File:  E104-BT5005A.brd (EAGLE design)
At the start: 15.5 x 15.5 mm, 5 parts

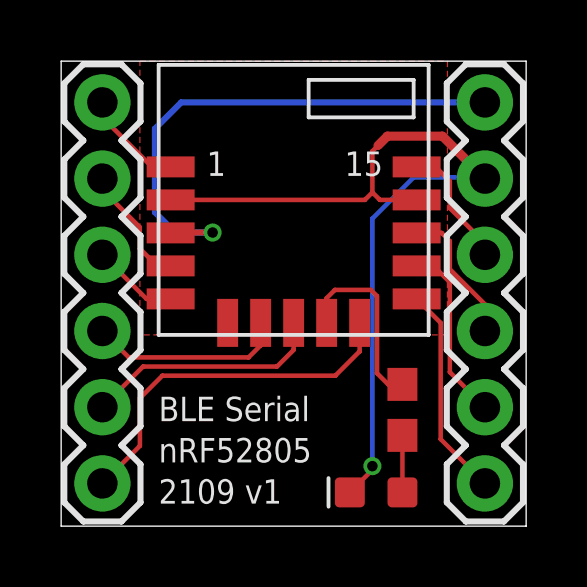
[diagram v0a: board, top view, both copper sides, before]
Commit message: v2 fixes, errors with part library
the original module library had errors. fixed module and silkscreen, added eagle library for ble module
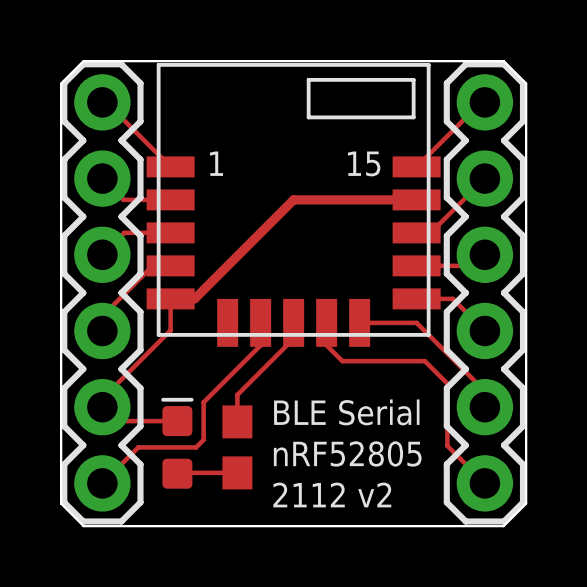
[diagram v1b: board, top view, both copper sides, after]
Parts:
- moved D1 6.79 mm to (4.00, 2.75), turned to 90 degrees
- moved R2 5.64 mm to (6.00, 2.75)
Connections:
- net DATA: now also J1.1; no longer J1.3
- net GND: now also J2.5; no longer J1.2
- net LINK: now also J1.2; no longer J1.4
- net MOD: now also J1.6; no longer J2.6
- net P0.01: now also J1.5; no longer J2.1
- net RST: now also J2.3; no longer J2.2
- net RX: now also J1.4; no longer J1.6
- net SWCLK: now also J2.2; no longer J2.3
- net SWDIO: now also J2.1; no longer J2.4
- net TX: now also J1.3; no longer J1.5
- net VCC: now also J2.4; no longer J1.1
- net WKP: now also J2.6; no longer J2.5
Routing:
- net VCC: track 17.8 -> 3.46 mm, vias 1 -> 0
- net GND: track 28.2 -> 16.8 mm, vias 1 -> 0
- net RX: track 7.09 -> 2.72 mm
- net TX: track 5.98 -> 2.43 mm
- net SWDIO: track 6.56 -> 3.17 mm
- net MOD: track 12.3 -> 9.15 mm
- net P0.00: track 6.28 -> 4.08 mm
- net P0.01: track 3.46 -> 5.65 mm
- net LINK: track 4.70 -> 3.02 mm
- net RST: track 4.12 -> 2.58 mm
- net DATA: track 4.24 -> 3.17 mm
- net WKP: track 8.07 -> 8.66 mm
- removed copper zone on layer 1, net GND
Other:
- outline, holes or cut-outs redrawn
- board text added: "2112 v2"
- board text removed: "2109 v1"
